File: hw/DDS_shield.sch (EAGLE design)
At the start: 32 parts, among them K1 mode, U1 ARDUINOR3-BPLACE, X1 F-out, X2 Input

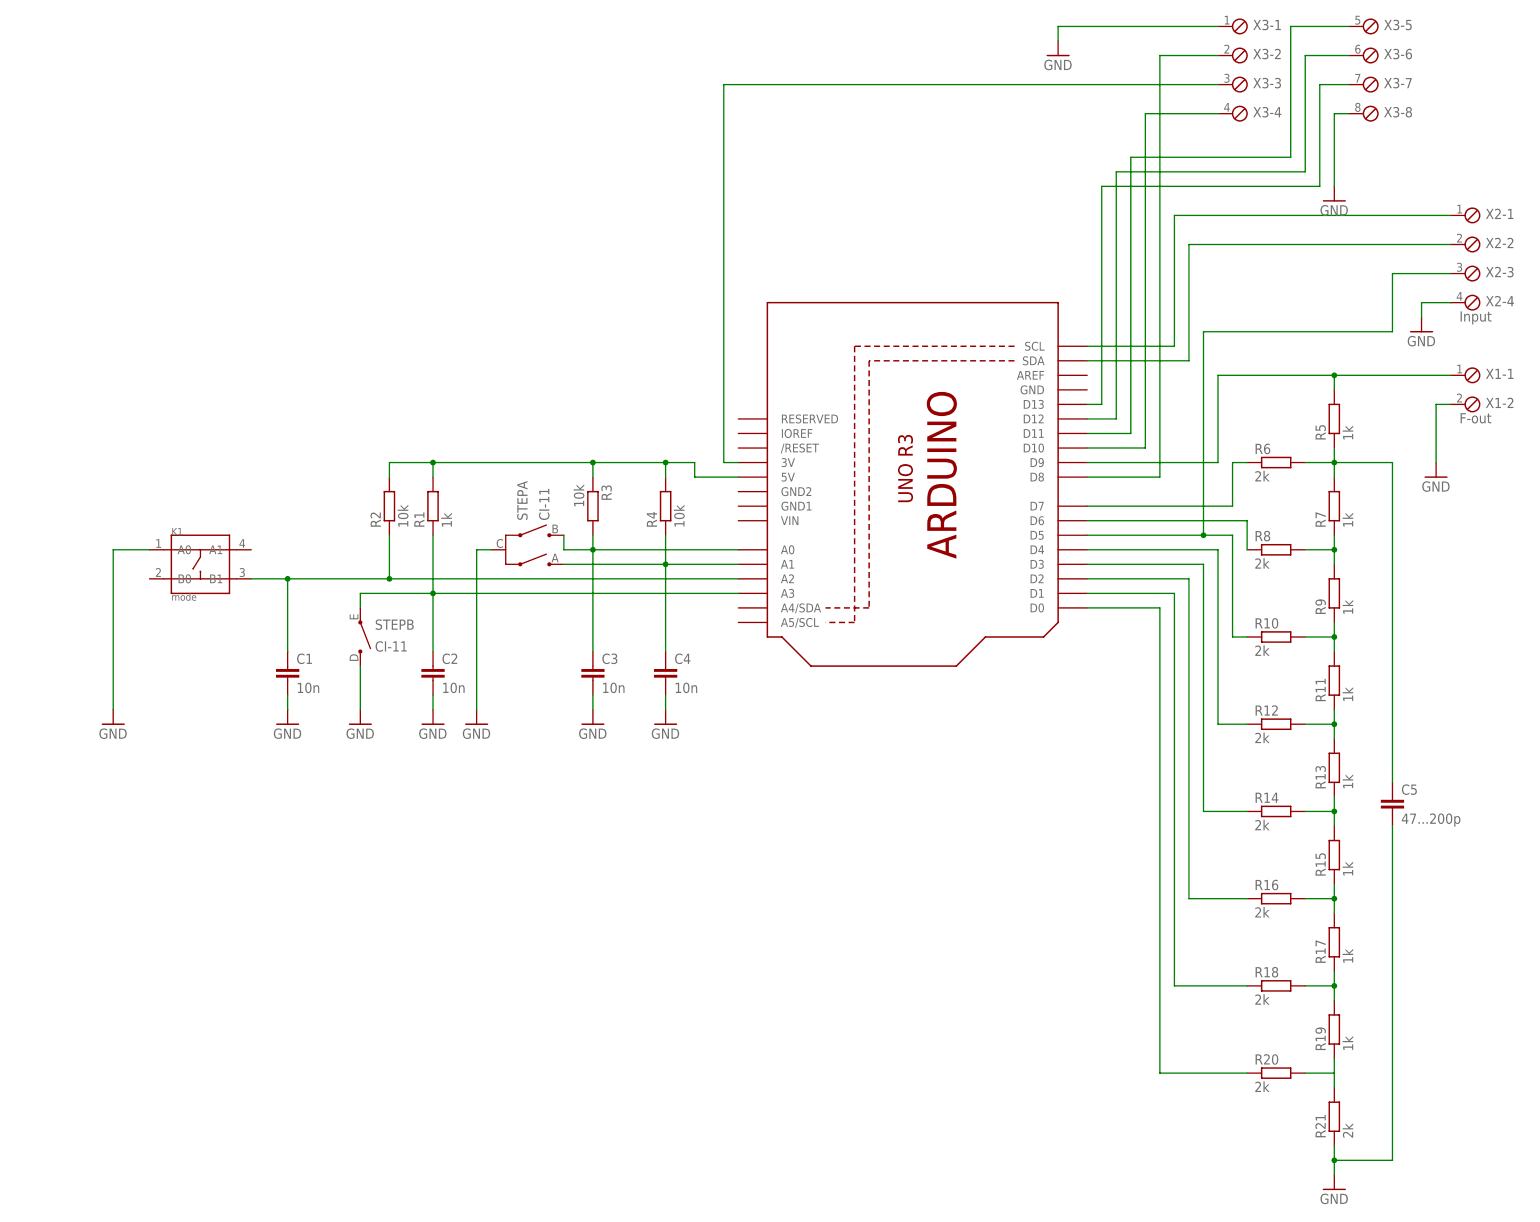
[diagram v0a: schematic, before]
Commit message: added extra ground terminals
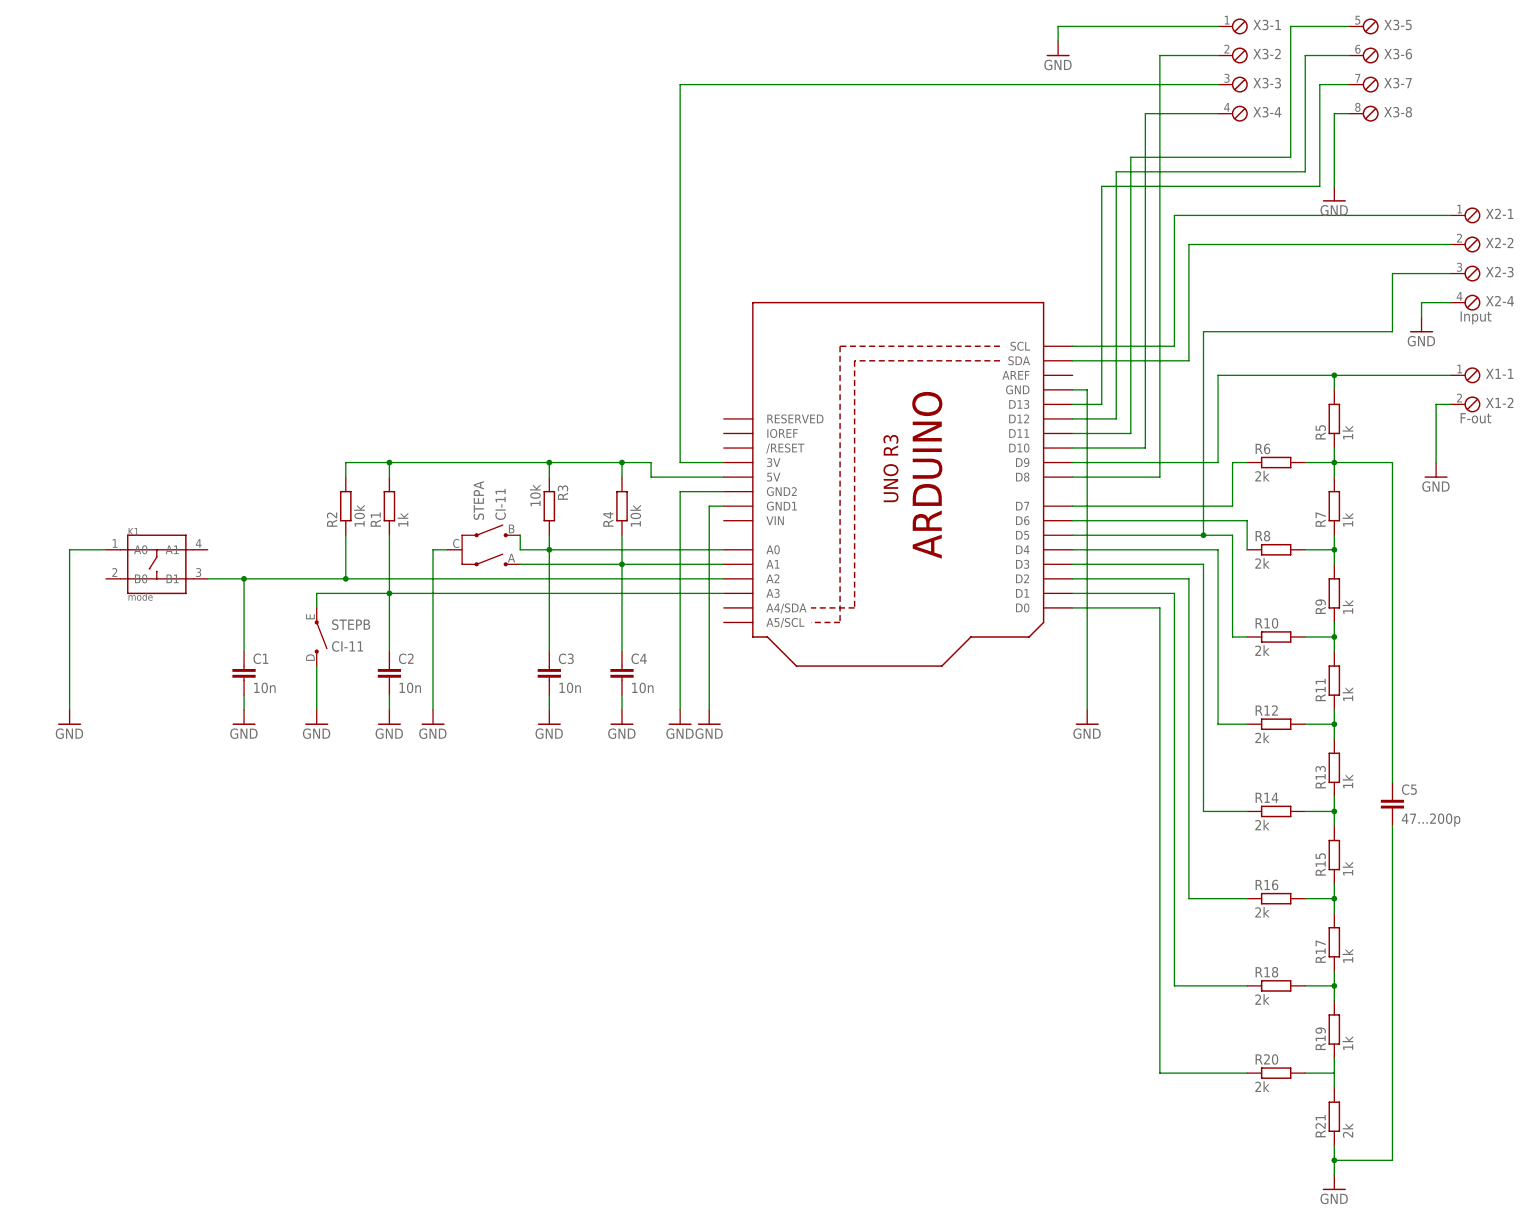
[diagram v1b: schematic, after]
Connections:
- net GND: now also U1.GND, U1.GND1, U1.GND2
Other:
- moved on the sheet: C1, C2, C3, C4, K1, R1, R2, R3, R4, STEPA, STEPB

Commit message: updated extra GNDs on schema
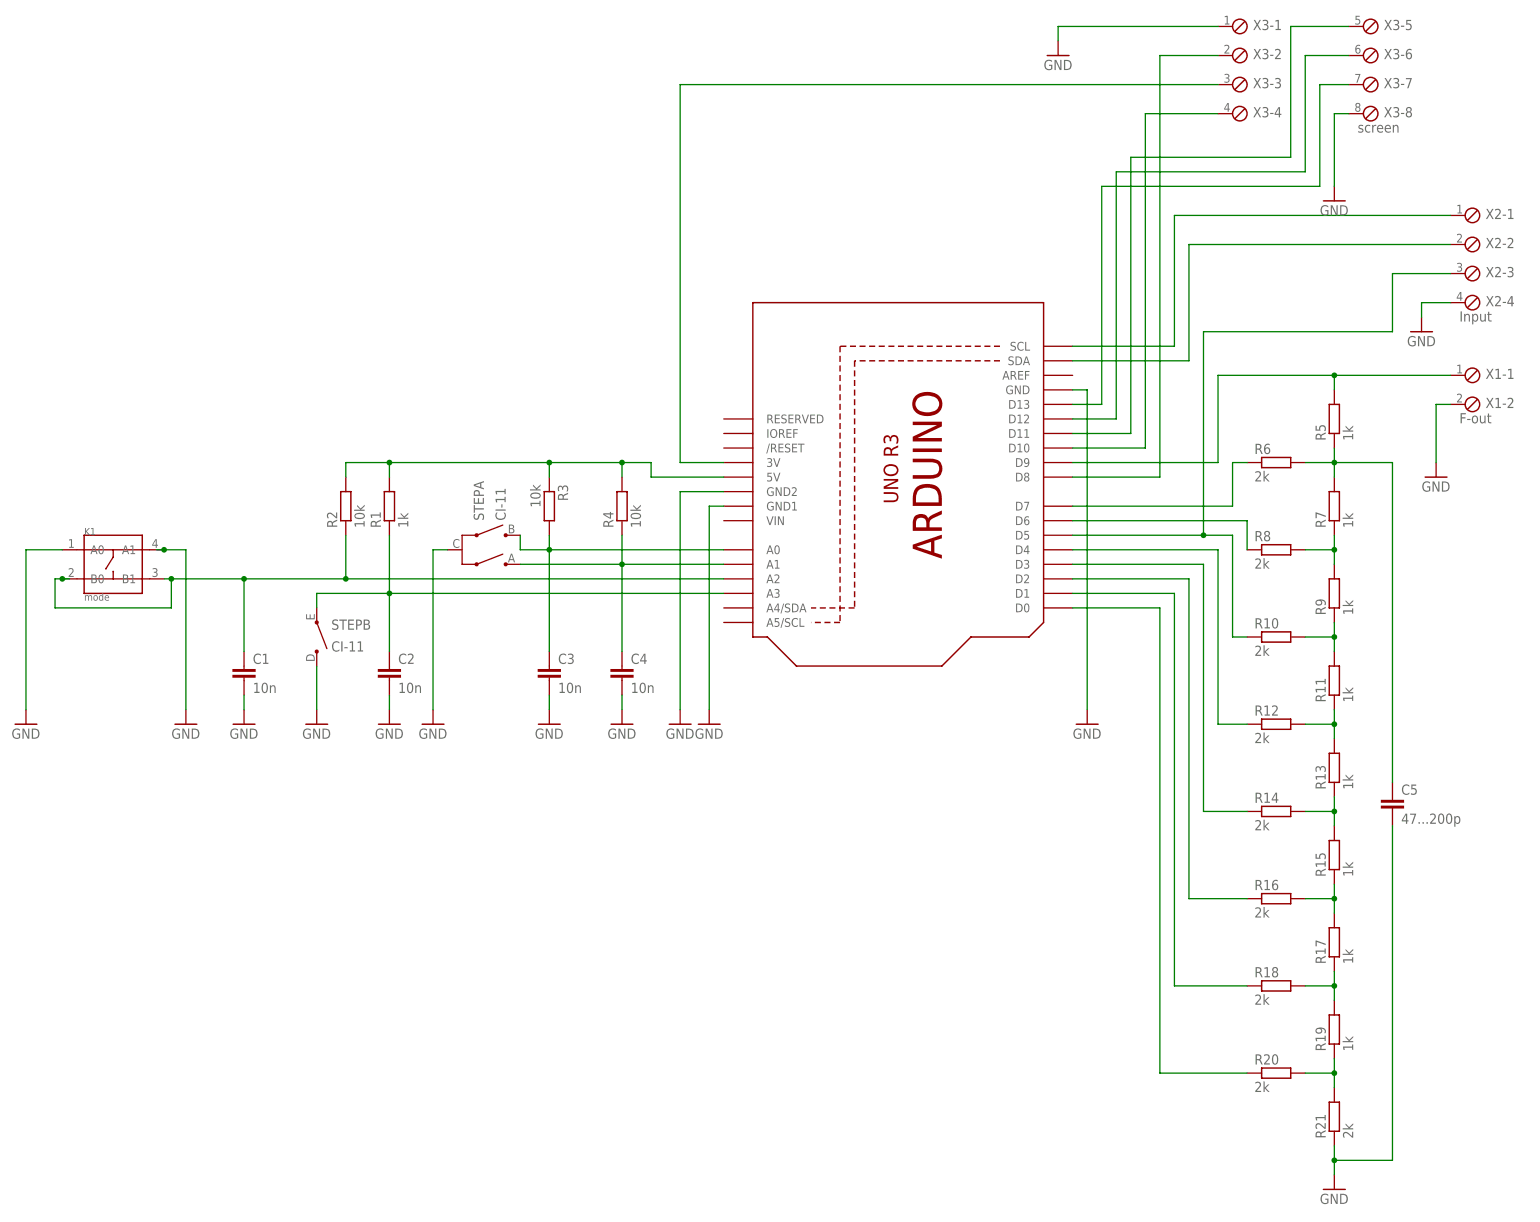
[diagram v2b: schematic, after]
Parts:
- X3: value (none) -> screen
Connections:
- net GND: now also K1.A1
- net N$1: now also K1.B0
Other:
- moved on the sheet: K1
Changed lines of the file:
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@@
 <part name="X1" library="con-phoenix-254" deviceset="MPT2" device="" value="F-out"/>
 <part name="X2" library="con-phoenix-254" deviceset="MPT4" device="" value="Input"/>
-<part name="X3" library="con-phoenix-254" deviceset="MPT8" device=""/>
+<part name="X3" library="con-phoenix-254" deviceset="MPT8" device="" value="screen"/>
 <part name="C5" library="rcl" deviceset="C-EU" device="C0805" value="47...200p"/>
 <part name="GND9" library="supply1" deviceset="GND" device=""/>
@@
 <part name="GND14" library="supply1" deviceset="GND" device=""/>
 <part name="GND15" library="supply1" deviceset="GND" device=""/>
+<part name="GND16" library="supply1" deviceset="GND" device=""/>
 </parts>
 <sheets>
@@
 <instance part="C3" gate="G$1" x="17.78" y="22.86"/>
 <instance part="C4" gate="G$1" x="30.48" y="22.86"/>
-<instance part="K1" gate="G$1" x="-50.8" y="40.64"/>
-<instance part="GND1" gate="1" x="-66.04" y="12.7"/>
+<instance part="K1" gate="G$1" x="-58.42" y="40.64"/>
+<instance part="GND1" gate="1" x="-73.66" y="12.7"/>
 <instance part="GND2" gate="1" x="-35.56" y="12.7"/>
 <instance part="GND3" gate="1" x="-22.86" y="12.7"/>
@@
 <instance part="GND14" gate="1" x="45.72" y="12.7"/>
 <instance part="GND15" gate="1" x="111.76" y="12.7"/>
+<instance part="GND16" gate="1" x="-45.72" y="12.7"/>
 </instances>
 <busses>
@@
 <segment>
 <pinref part="GND1" gate="1" pin="GND"/>
-<wire x1="-66.04" y1="15.24" x2="-66.04" y2="43.18" width="0.1524" layer="91"/>
-<wire x1="-66.04" y1="43.18" x2="-59.69" y2="43.18" width="0.1524" layer="91"/>
+<wire x1="-73.66" y1="15.24" x2="-73.66" y2="43.18" width="0.1524" layer="91"/>
+<wire x1="-73.66" y1="43.18" x2="-67.31" y2="43.18" width="0.1524" layer="91"/>
 <pinref part="K1" gate="G$1" pin="A0"/>
 </segment>
@@
 <wire x1="111.76" y1="71.12" x2="111.76" y2="15.24" width="0.1524" layer="91"/>
 </segment>
+<segment>
+<wire x1="-50.8" y1="43.18" x2="-49.53" y2="43.18" width="0.1524" layer="91"/>
+<wire x1="-49.53" y1="43.18" x2="-45.72" y2="43.18" width="0.1524" layer="91"/>
+<wire x1="-45.72" y1="43.18" x2="-45.72" y2="15.24" width="0.1524" layer="91"/>
+<pinref part="GND16" gate="1" pin="GND"/>
+<pinref part="K1" gate="G$1" pin="A1"/>
+<junction x="-49.53" y="43.18"/>
+</segment>
 </net>
 <net name="N$1" class="0">
@@
 <wire x1="-35.56" y1="38.1" x2="-35.56" y2="25.4" width="0.1524" layer="91"/>
 <pinref part="K1" gate="G$1" pin="B1"/>
-<wire x1="-41.91" y1="38.1" x2="-35.56" y2="38.1" width="0.1524" layer="91"/>
+<wire x1="-49.53" y1="38.1" x2="-48.26" y2="38.1" width="0.1524" layer="91"/>
 <junction x="-35.56" y="38.1"/>
 <pinref part="R2" gate="G$1" pin="1"/>
+<wire x1="-48.26" y1="38.1" x2="-35.56" y2="38.1" width="0.1524" layer="91"/>
 <wire x1="-17.78" y1="45.72" x2="-17.78" y2="38.1" width="0.1524" layer="91"/>
 <junction x="-17.78" y="38.1"/>
+<wire x1="-66.04" y1="38.1" x2="-67.31" y2="38.1" width="0.1524" layer="91"/>
+<wire x1="-67.31" y1="38.1" x2="-68.58" y2="38.1" width="0.1524" layer="91"/>
+<wire x1="-68.58" y1="38.1" x2="-68.58" y2="33.02" width="0.1524" layer="91"/>
+<wire x1="-68.58" y1="33.02" x2="-48.26" y2="33.02" width="0.1524" layer="91"/>
+<wire x1="-48.26" y1="33.02" x2="-48.26" y2="38.1" width="0.1524" layer="91"/>
+<pinref part="K1" gate="G$1" pin="B0"/>
+<junction x="-67.31" y="38.1"/>
+<junction x="-48.26" y="38.1"/>
 </segment>
 </net>
@@
 <wire x1="154.94" y1="-48.26" x2="154.94" y2="-50.8" width="0.1524" layer="91"/>
 <wire x1="149.86" y1="-48.26" x2="154.94" y2="-48.26" width="0.1524" layer="91"/>
+<junction x="154.94" y="-48.26"/>
 </segment>
 </net>
@@
 </sheet>
 </sheets>
+<errors>
+</errors>
 </schematic>
 </drawing>
